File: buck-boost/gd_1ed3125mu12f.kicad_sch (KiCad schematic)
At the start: 16 parts, among them U1 1ED3125MU12F

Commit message: Working on power stage of buck-boost plat
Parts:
- C1: value 10uF -> 1uF
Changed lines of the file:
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@@
 			)
 		)
-		(property "Value" "10uF"
+		(property "Value" "1uF"
 			(at 36.83 48.26 0)
 			(effects

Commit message: Schematics for power stage
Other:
- note removed: "Add test points"
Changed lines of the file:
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@@
-		)
-	)
-	(text "Add test points"
-		(exclude_from_sim no)
-		(at 146.812 83.566 0)
-		(effects
-			(font
-				(size 1.27 1.27)
-			)
 		)
 	)

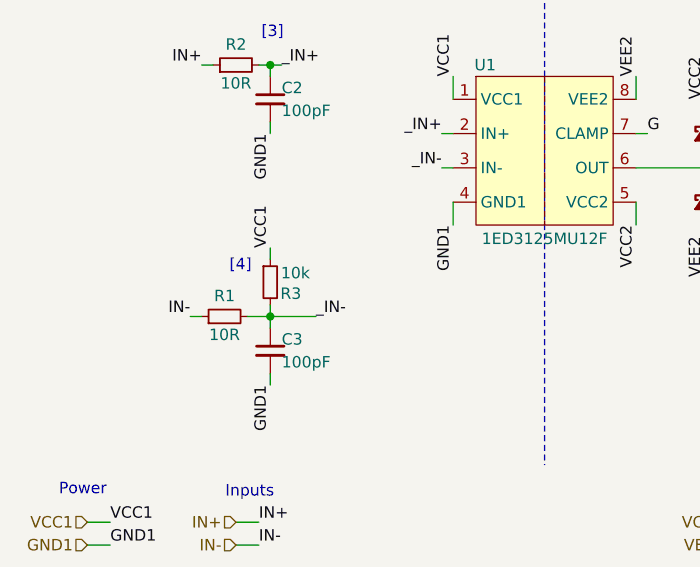
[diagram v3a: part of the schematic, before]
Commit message: Added load switch and relay drivers
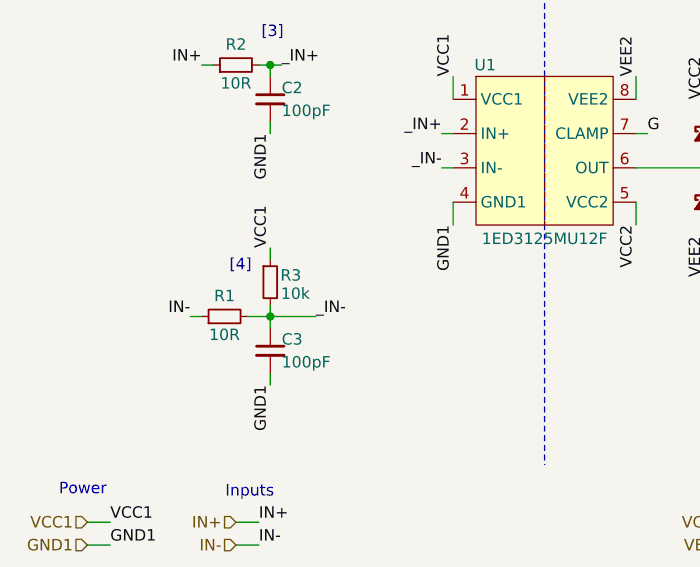
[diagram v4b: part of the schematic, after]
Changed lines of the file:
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@@
 		(dnp no)
 		(property "Reference" "R3"
-			(at 42.926 86.36 0)
+			(at 42.926 84.328 0)
 			(effects
 				(font
@@
 		)
 		(property "Value" "10k"
-			(at 43.434 84.074 0)
+			(at 43.434 86.36 0)
 			(effects
 				(font

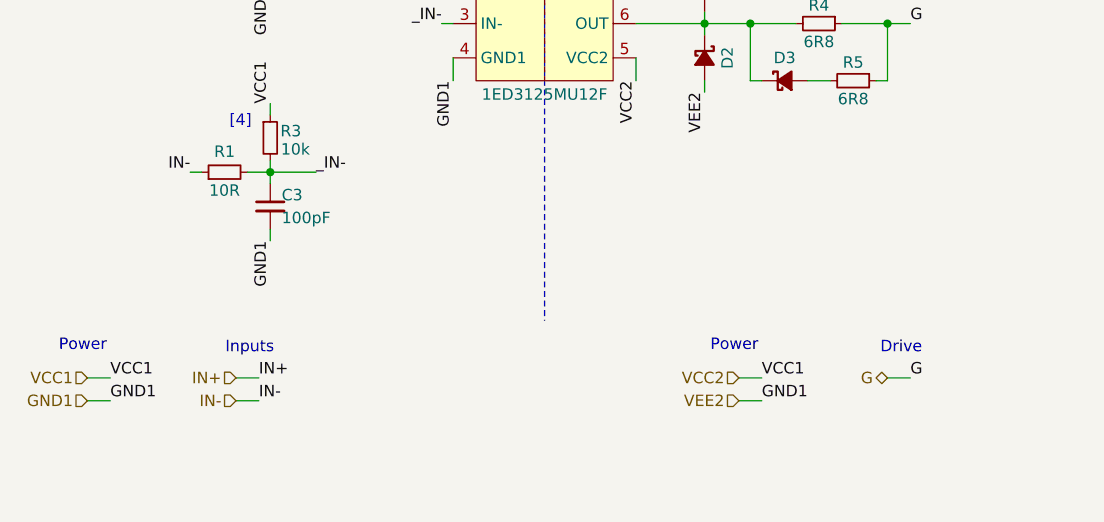
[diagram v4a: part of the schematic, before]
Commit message: Adding connectors, test points to gate drivers
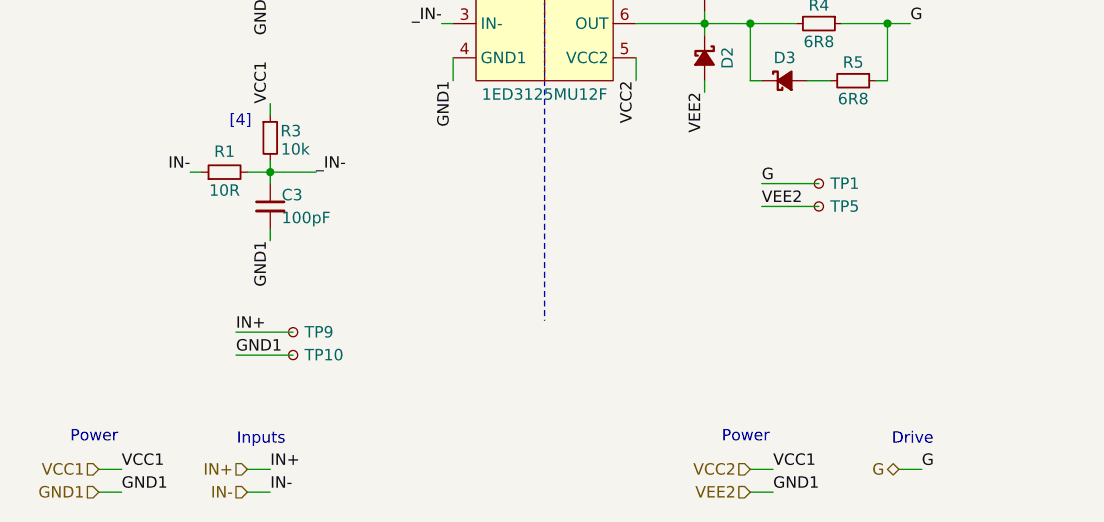
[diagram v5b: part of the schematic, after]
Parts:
- added TP1, TP10, TP5, TP9: TestPoint_Small, Connector_PinHeader_2.54mm:PinHeader_1x01_P2.54mm_Vertical, symbol Connector:TestPoint_Small
- D1, D2, D3: footprint (none) -> Diode_SMD:D_SOD-123
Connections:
- net G: now also TP1.1
- net GND1: now also TP10.1, TP5.1
- net IN+: now also TP9.1

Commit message: Adding current and voltage measurements blocks
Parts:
- renumbered TP1 to TP?
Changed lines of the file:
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@@
 		(on_board yes)
 		(dnp no)
-		(property "Reference" "TP1"
+		(property "Reference" "TP?"
 			(at 102.87 90.1699 0)
 			(effects
@@
 		)
 		(instances
-			(project ""
+			(project "buck-boost-xp"
 				(path "/3f994017-d36f-4c43-a8c8-740bd919e8ad/fdca222d-0f97-4e31-8037-fff4f850ee1b/761151f6-faee-4ce9-9368-5feaea030452"
-					(reference "TP1")
+					(reference "TP?")
 					(unit 1)
 				)
 				(path "/3f994017-d36f-4c43-a8c8-740bd919e8ad/fdca222d-0f97-4e31-8037-fff4f850ee1b/84d1d1f7-2f54-4c33-9a3e-2e9dd13843c7"
-					(reference "TP3")
+					(reference "TP?")
 					(unit 1)
 				)
 				(path "/3f994017-d36f-4c43-a8c8-740bd919e8ad/fdca222d-0f97-4e31-8037-fff4f850ee1b/a54d3f19-6e2c-4865-abea-187ad4200fd2"
-					(reference "TP4")
+					(reference "TP?")
 					(unit 1)
 				)
 				(path "/3f994017-d36f-4c43-a8c8-740bd919e8ad/fdca222d-0f97-4e31-8037-fff4f850ee1b/ae7b56dd-c12d-4359-b01b-e816c6964e9d"
-					(reference "TP2")
+					(reference "TP?")
 					(unit 1)
 				)

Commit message: The changes indicated in the text document Review. 05.11.2024 were implemented. Missing footprints were added
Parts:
- gave numbers to parts that had none: 1
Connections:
- net GND1: no longer C5.2, C6.2, C7.2, D2.2 (A), TP5.1, U1.8 (VEE2)
- net VCC1: no longer C5.1, C6.1, C7.1, D1.1 (K), U1.5 (VCC2)
- new net VCC2: C5.1, C6.1, C7.1, D1.1 (K), U1.5 (VCC2)
- new net VEE2: C5.2, C6.2, C7.2, D2.2 (A), TP5.1, U1.8 (VEE2)
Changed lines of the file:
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@@
-		)
-	)
-	(label "GND1"
-		(at 96.52 124.46 0)
-		(fields_autoplaced yes)
-		(effects
-			(font
-				(size 1.27 1.27)
-			)
-			(justify left bottom)
 		)
 	)
@@
 		)
 	)
+	(label "VEE2"
+		(at 96.52 124.46 0)
+		(fields_autoplaced yes)
+		(effects
+			(font
+				(size 1.27 1.27)
+			)
+			(justify left bottom)
+		)
+	)
 	(label "VCC1"
 		(at 40.64 81.28 90)
@@
 		)
 	)
-	(label "VCC1"
-		(at 96.52 121.92 0)
-		(fields_autoplaced yes)
-		(effects
-			(font
-				(size 1.27 1.27)
-			)
-			(justify left bottom)
-		)
-	)
 	(label "GND1"
 		(at 60.96 78.74 270)
@@
 			)
 			(justify right bottom)
+		)
+	)
+	(label "VCC2"
+		(at 96.52 121.92 0)
+		(fields_autoplaced yes)
+		(effects
+			(font
+				(size 1.27 1.27)
+			)
+			(justify left bottom)
 		)
 	)
@@
 		(on_board yes)
 		(dnp no)
-		(property "Reference" "TP?"
+		(property "Reference" "TP1"
 			(at 102.87 90.1699 0)
 			(effects
@@
 			(project "buck-boost-xp"
 				(path "/3f994017-d36f-4c43-a8c8-740bd919e8ad/fdca222d-0f97-4e31-8037-fff4f850ee1b/761151f6-faee-4ce9-9368-5feaea030452"
-					(reference "TP?")
+					(reference "TP1")
 					(unit 1)
 				)
 				(path "/3f994017-d36f-4c43-a8c8-740bd919e8ad/fdca222d-0f97-4e31-8037-fff4f850ee1b/84d1d1f7-2f54-4c33-9a3e-2e9dd13843c7"
-					(reference "TP?")
+					(reference "TP3")
 					(unit 1)
 				)
 				(path "/3f994017-d36f-4c43-a8c8-740bd919e8ad/fdca222d-0f97-4e31-8037-fff4f850ee1b/a54d3f19-6e2c-4865-abea-187ad4200fd2"
-					(reference "TP?")
+					(reference "TP4")
 					(unit 1)
 				)
 				(path "/3f994017-d36f-4c43-a8c8-740bd919e8ad/fdca222d-0f97-4e31-8037-fff4f850ee1b/ae7b56dd-c12d-4359-b01b-e816c6964e9d"
-					(reference "TP?")
-					(unit 1)
-				)
+					(reference "TP2")
+					(unit 1)
+				)

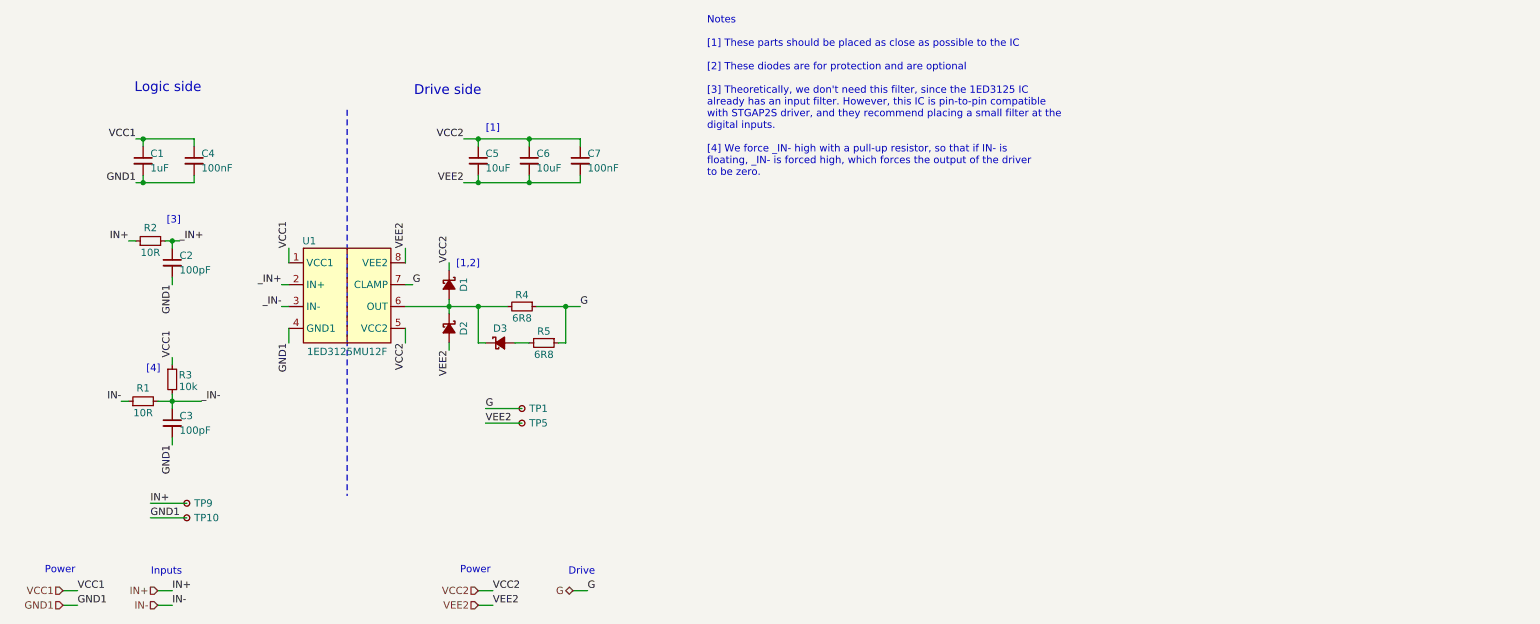
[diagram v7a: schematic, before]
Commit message: Some errors in the schematics were corrected. PCB file V1.0
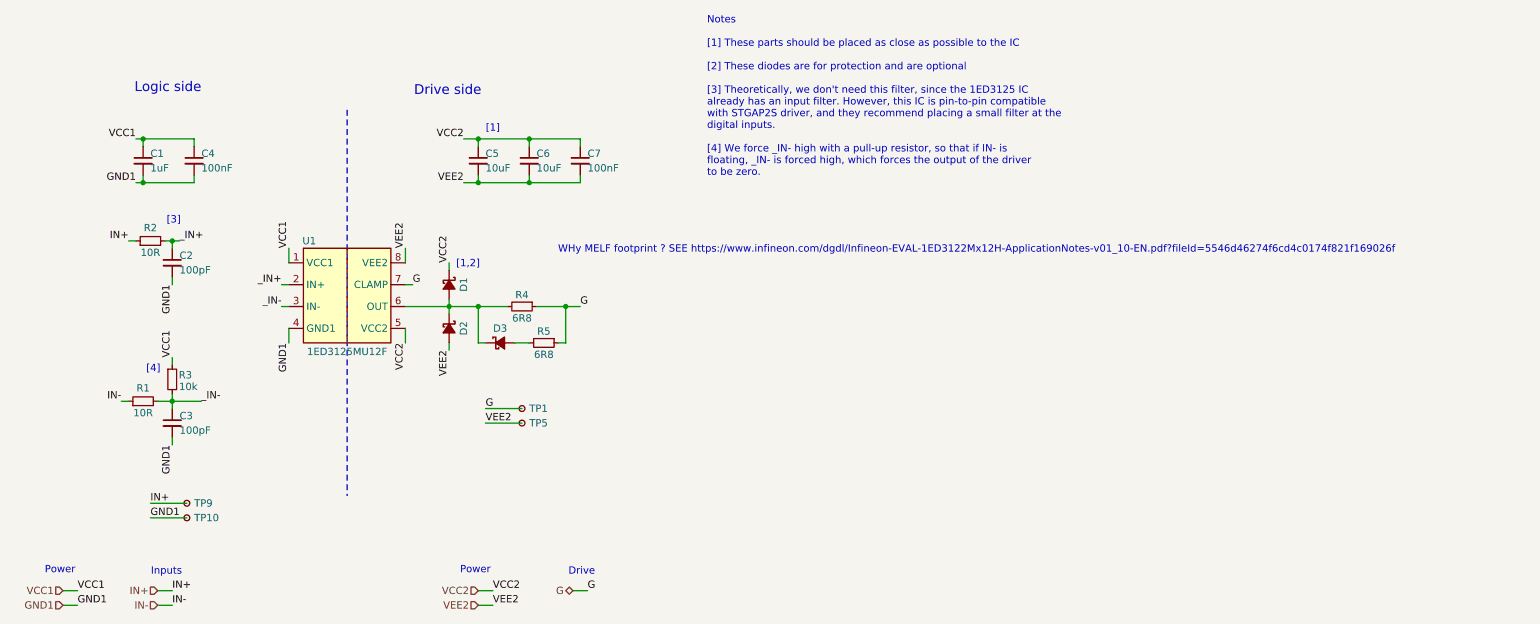
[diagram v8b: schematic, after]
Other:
- note added: "WHy MELF footprint ? SEE https://www.infineon.com/dgdl/Infineon-EVAL-1ED3122Mx12H-ApplicationNotes-v01_10-EN.pdf?fileId=5546d46274f6cd4c0174f821f169026f"
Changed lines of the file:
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@@
+		)
+	)
+	(text "WHy MELF footprint ? SEE https://www.infineon.com/dgdl/Infineon-EVAL-1ED3122Mx12H-ApplicationNotes-v01_10-EN.pdf?fileId=5546d46274f6cd4c0174f821f169026f\n"
+		(exclude_from_sim no)
+		(at 180.848 62.484 0)
+		(effects
+			(font
+				(size 1.27 1.27)
+			)
 		)
 	)
